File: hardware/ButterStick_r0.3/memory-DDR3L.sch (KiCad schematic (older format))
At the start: 3 parts, among them U4 MT41K64M16TW-107_J-TR, U5 MT41K64M16TW-107_J-TR, U6 S25FL127S

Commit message: hw.r0_3: Experiment with buses
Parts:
- removed U4, U5: MT41K64M16TW-107_J-TR, Package_BGA:BGA-96_9.0x13.0mm_Layout2x3x16_P0.8mm, symbol gkl_mem:MT41K64M16TW-107_J-TR
- removed U6: S25FL127S, Package_SO:SOIJ-8_5.3x5.3mm_P1.27mm, symbol gkl_mem:AT25SF081
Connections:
- net labels added: DRAM0{DRAM_DAT0}, DRAM1{DRAM_DAT0}, DRAM{DRAM_CTRL}
- net labels removed: +3V3, ADR0, ADR1, ADR10, ADR11, ADR12, ADR13, ADR14, ADR15, ADR2, ADR3, ADR4, ADR5, ADR6, ADR7, ADR8, ADR9, BA0, BA1, BA2, CAS, CKE, CK_N, CK_P, CS, DQ0, DQ1, DQ10, DQ11, DQ12, DQ13, DQ14, DQ15, DQ16, DQ17, DQ18, DQ19, DQ2, DQ20, DQ21, DQ22, DQ23, DQ24, DQ25, DQ26, DQ27, DQ28, DQ29, DQ3, DQ30, DQ31, DQ4, DQ5, DQ6, DQ7, DQ8, DQ9, GND, LDM, LDQS_N, LDQS_P, ODT, P_1.35_DRAM, QSPI_D2, QSPI_D3, RAS, RESET, SPI_CONFIG_MISO, SPI_CONFIG_MOSI, SPI_CONFIG_SCK, SPI_CONFIG_SS, UDM, UDQS_N, UDQS_P, WE, {DRAM_CTRL}, {DRAM_DAT0}, {DRAM_DAT1}
- wire segments 104 -> 0

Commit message: hw.r0_3: cleanup and additions
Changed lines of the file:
@@
 $Descr A4 11693 8268
 encoding utf-8
-Sheet 4 16
+Sheet 16 20
 Title "ButterStick"
 Date "2019-06-14"
@@
 Comment9 ""
 $EndDescr
-Connection ~ 3650 1950
+Connection ~ 3550 2950
 Wire Bus Line
-	3500 1950 3650 1950
+	3400 2950 3550 2950
 Wire Bus Line
-	3650 1950 6400 1950
+	3550 2950 6300 2950
 Wire Bus Line
-	3650 2250 3650 1950
+	3550 3250 3550 2950
 Wire Bus Line
-	3700 2550 3800 2550
+	3600 3550 3700 3550
 Wire Bus Line
-	3800 2250 3650 2250
+	3700 3250 3550 3250
 Wire Bus Line
-	6400 1950 6400 2250
+	6300 2950 6300 3250
 Wire Bus Line
-	6400 2250 6600 2250
+	6300 3250 6500 3250
 Wire Bus Line
-	6500 2550 6600 2550
-Text HLabel 3500 1950 0    50   Input ~ 10
+	6400 3550 6500 3550
+Text HLabel 3400 2950 0    50   Input ~ 10
 DRAM{DRAM_CTRL}
-Text HLabel 3700 2550 0    50   Input ~ 10
+Text HLabel 3600 3550 0    50   Input ~ 10
 DRAM0{DRAM_DAT0}
-Text HLabel 6500 2550 0    50   Input ~ 10
+Text HLabel 6400 3550 0    50   Input ~ 10
 DRAM1{DRAM_DAT0}
 $Sheet
-S 6600 2150 1800 1150
+S 6500 3150 1800 1150
 U 5EB15CF3
 F0 "DDR3L" 50
 F1 "DDR3L.sch" 50
-F2 "DRAM{DRAM_DAT0}" I L 6600 2550 50
-F3 "DRAM{DRAM_CTRL}" I L 6600 2250 50
+F2 "DRAM{DRAM_DAT0}" I L 6500 3550 50
+F3 "DRAM{DRAM_CTRL}" I L 6500 3250 50
 $EndSheet
 $Sheet
-S 3800 2150 1800 1150
+S 3700 3150 1800 1150
 U 5EB207D6
 F0 "DDR3L1" 50
 F1 "DDR3L.sch" 50
-F2 "DRAM{DRAM_DAT0}" I L 3800 2550 50
-F3 "DRAM{DRAM_CTRL}" I L 3800 2250 50
+F2 "DRAM{DRAM_DAT0}" I L 3700 3550 50
+F3 "DRAM{DRAM_CTRL}" I L 3700 3250 50
 $EndSheet
 $EndSCHEMATC

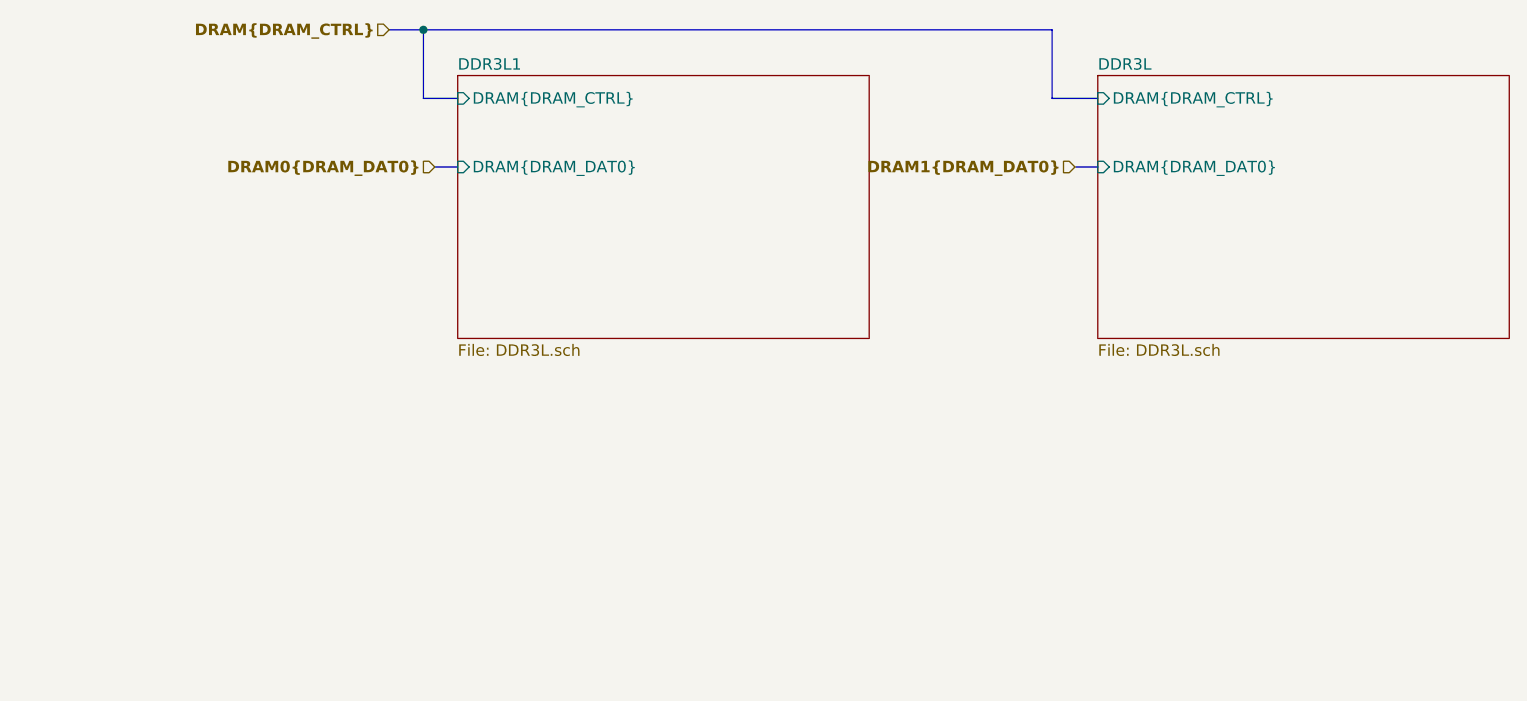
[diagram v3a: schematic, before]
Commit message: hw.r0_3: Start pin assignments for DDR3
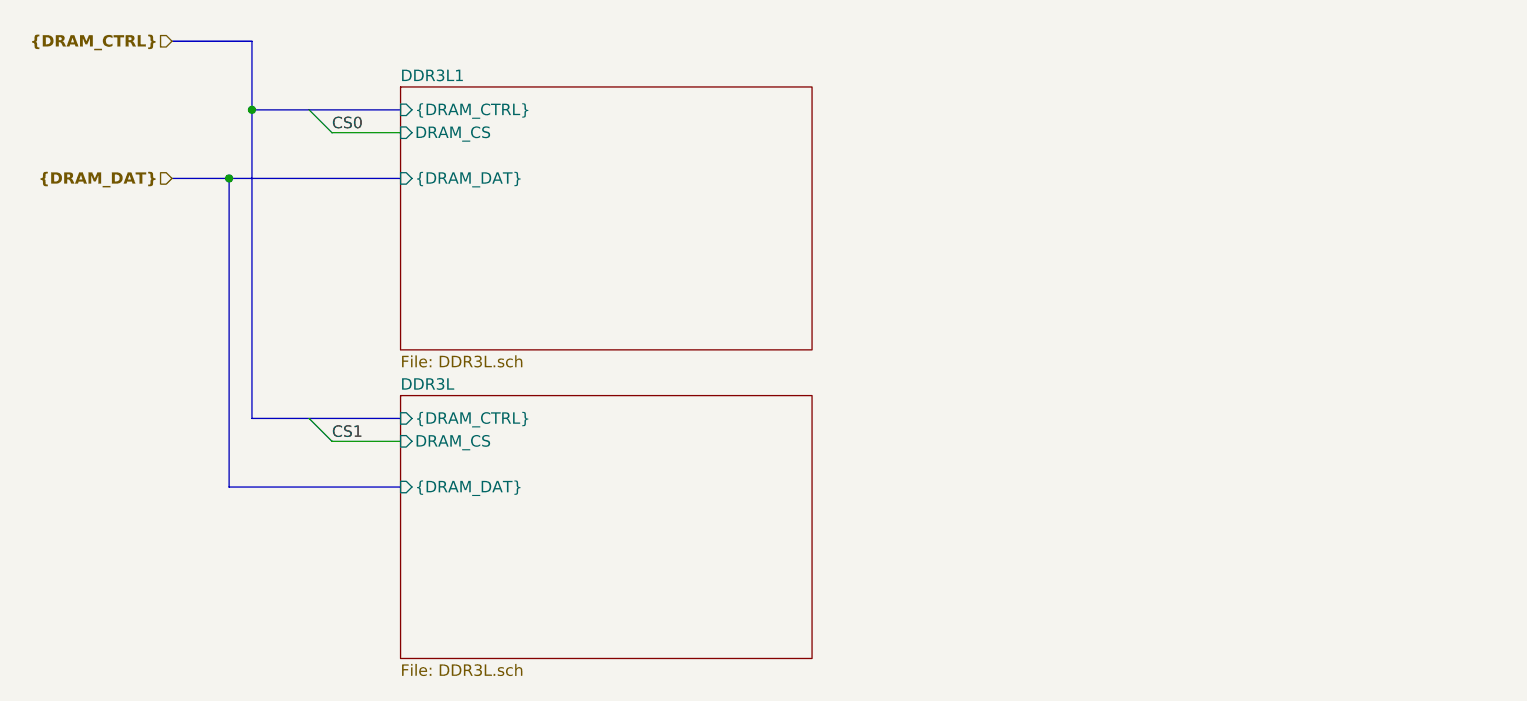
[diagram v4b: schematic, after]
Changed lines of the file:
@@
 $Descr A4 11693 8268
 encoding utf-8
-Sheet 2 18
+Sheet 3 20
 Title "ButterStick"
 Date "2019-06-14"
@@
 Comment9 ""
 $EndDescr
-Connection ~ 3550 2950
+Connection ~ 2800 3300
+Connection ~ 2700 3600
+Entry Wire Line
+	3050 3300 3150 3400
+Entry Wire Line
+	3050 4650 3150 4750
+Wire Wire Line
+	3150 3400 3450 3400
+Wire Wire Line
+	3150 4750 3450 4750
 Wire Bus Line
-	3400 2950 3550 2950
+	2450 3000 2800 3000
 Wire Bus Line
-	3550 2950 6300 2950
+	2450 3600 2700 3600
 Wire Bus Line
-	3550 3250 3550 2950
+	2700 3600 2700 4950
 Wire Bus Line
-	3600 3550 3700 3550
+	2700 3600 3450 3600
 Wire Bus Line
-	3700 3250 3550 3250
+	2700 4950 3450 4950
 Wire Bus Line
-	6300 2950 6300 3250
+	2800 3300 2800 3000
 Wire Bus Line
-	6300 3250 6500 3250
+	2800 3300 2800 4650
 Wire Bus Line
-	6400 3550 6500 3550
-Text HLabel 3400 2950 0    50   Input ~ 10
-DRAM{DRAM_CTRL}
-Text HLabel 3600 3550 0    50   Input ~ 10
-DRAM0{DRAM_DAT0}
-Text HLabel 6400 3550 0    50   Input ~ 10
-DRAM1{DRAM_DAT0}
+	2800 3300 3450 3300
+Wire Bus Line
+	2800 4650 3450 4650
+Text Label 3150 3400 0    50   ~ 0
+CS0
+Text Label 3150 4750 0    50   ~ 0
+CS1
+Text HLabel 2450 3000 0    50   Input ~ 10
+{DRAM_CTRL}
+Text HLabel 2450 3600 0    50   Input ~ 10
+{DRAM_DAT}
 $Sheet
-S 6500 3150 1800 1150
+S 3450 4550 1800 1150
 U 5EB15CF3
 F0 "DDR3L" 50
 F1 "DDR3L.sch" 50
-F2 "DRAM{DRAM_DAT0}" I L 6500 3550 50
-F3 "DRAM{DRAM_CTRL}" I L 6500 3250 50
+F2 "{DRAM_DAT}" I L 3450 4950 50
+F3 "{DRAM_CTRL}" I L 3450 4650 50
+F4 "DRAM_CS" I L 3450 4750 50
 $EndSheet
 $Sheet
-S 3700 3150 1800 1150
+S 3450 3200 1800 1150
 U 5EB207D6
 F0 "DDR3L1" 50
 F1 "DDR3L.sch" 50
-F2 "DRAM{DRAM_DAT0}" I L 3700 3550 50
-F3 "DRAM{DRAM_CTRL}" I L 3700 3250 50
+F2 "{DRAM_DAT}" I L 3450 3600 50
+F3 "{DRAM_CTRL}" I L 3450 3300 50
+F4 "DRAM_CS" I L 3450 3400 50
 $EndSheet
 $EndSCHEMATC
